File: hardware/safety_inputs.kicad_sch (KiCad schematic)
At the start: 28 parts, among them U11 TLP291-4, U8 TLP291-4, U9 TLP291-4

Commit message: Add the Cube project
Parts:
- added R?: 0R, Resistor_SMD:R_0402_1005Metric, symbol Device:R_Small
- added U10: TCA6416ARTWR, QFN50P400X400X80-25N, symbol TCA6416ARTWR:TCA6416ARTWR
- R? (x12): value 100R -> 2k
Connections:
- net +3.3V: now also U10.21 (VCCP), U10.23 (VCCI)
- net GND: now also R?.1, U10.25 (EP), U10.9 (GND)
- net OUT_ASMS: now also U10.15 (P15)
- net OUT_FW: now also U10.14 (P14)
- net OUT_HV: now also U10.13 (P13)
- net OUT_HVD: now also U10.11 (P11)
- net OUT_INV: now also U10.10 (P10)
- net OUT_RES: now also U10.12 (P12)
- net OUT_RFU1: now also U10.16 (P16)
- net OUT_RFU2: now also U10.17 (P17)
- net OUT_W_FL: now also U10.1 (P00)
- net OUT_W_FR: now also U10.2 (P01)
- net OUT_W_RL: now also U10.3 (P02)
- net OUT_W_RR: now also U10.4 (P03)
- net IN_W_FL renamed IN_WHEEL_FL
- net IN_W_FR renamed IN_WHEEL_FR
- net IN_W_RL renamed IN_WHEEL_RL
- net IN_W_RR renamed IN_WHEEL_RR
- new net: R?.2, U10.18 (ADDR)
- new net LED_CAN: U10.5 (P04)
- new net LED_ERROR: U10.6 (P05)
- new net LED_FUSE: U10.8 (P07)
- new net LED_SAFETY: U10.7 (P06)
- new net SCL: U10.19 (SCL)
- new net SDA: U10.20 (SDA)
- new net ~{INT}: U10.22 (~{INT})
- new net ~{RESET}: U10.24 (~{RESET})
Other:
- note added: "Status LEDs"
- note removed: "ASMS"
- note removed: "FW"
- note removed: "HV"
- note removed: "HVD"
- note removed: "INV"
- note removed: "Larger diode resistor?"
- note removed: "RES"
- note removed: "WHEEL FL"
- note removed: "WHEEL FR"
- note removed: "WHEEL RL"
- note removed: "WHEEL RR"
- title: (none) -> Safety Inputs
- moved on the sheet: R?, U11A, U11B, U11C, U11D, U8A, U8B, U8D, U9A, U9B, U9C, U9D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

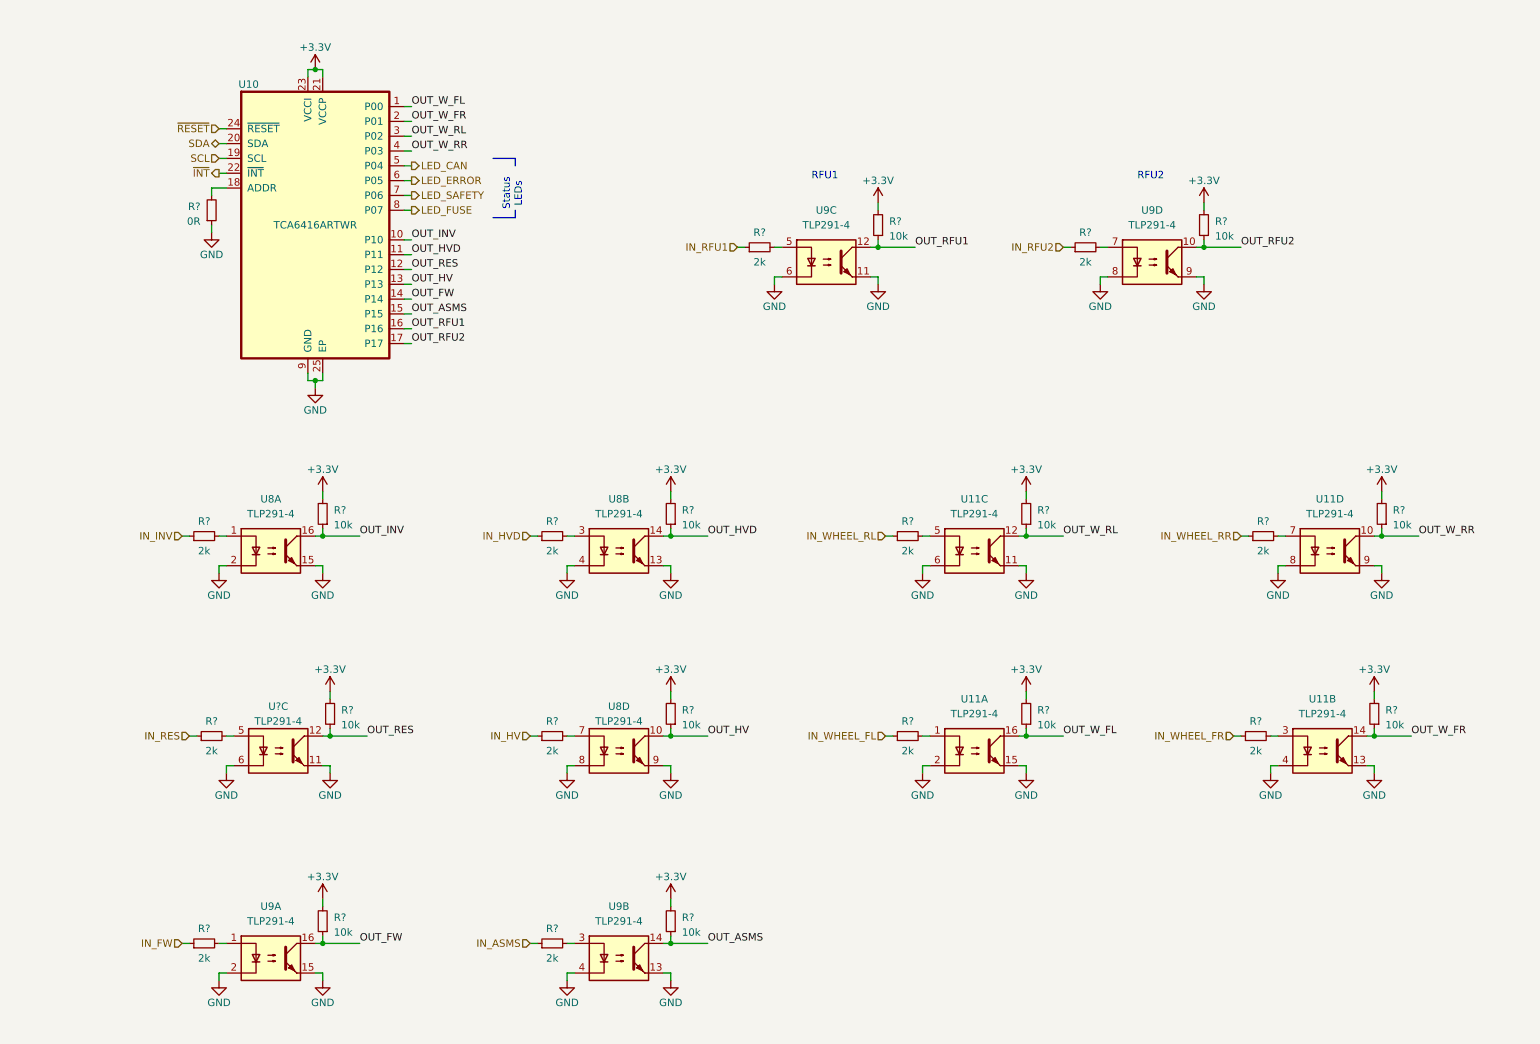
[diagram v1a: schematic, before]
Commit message: Improve the schematic
- add anti-aliasing filters
- rearrange the main connector signals
- improve the power filtering
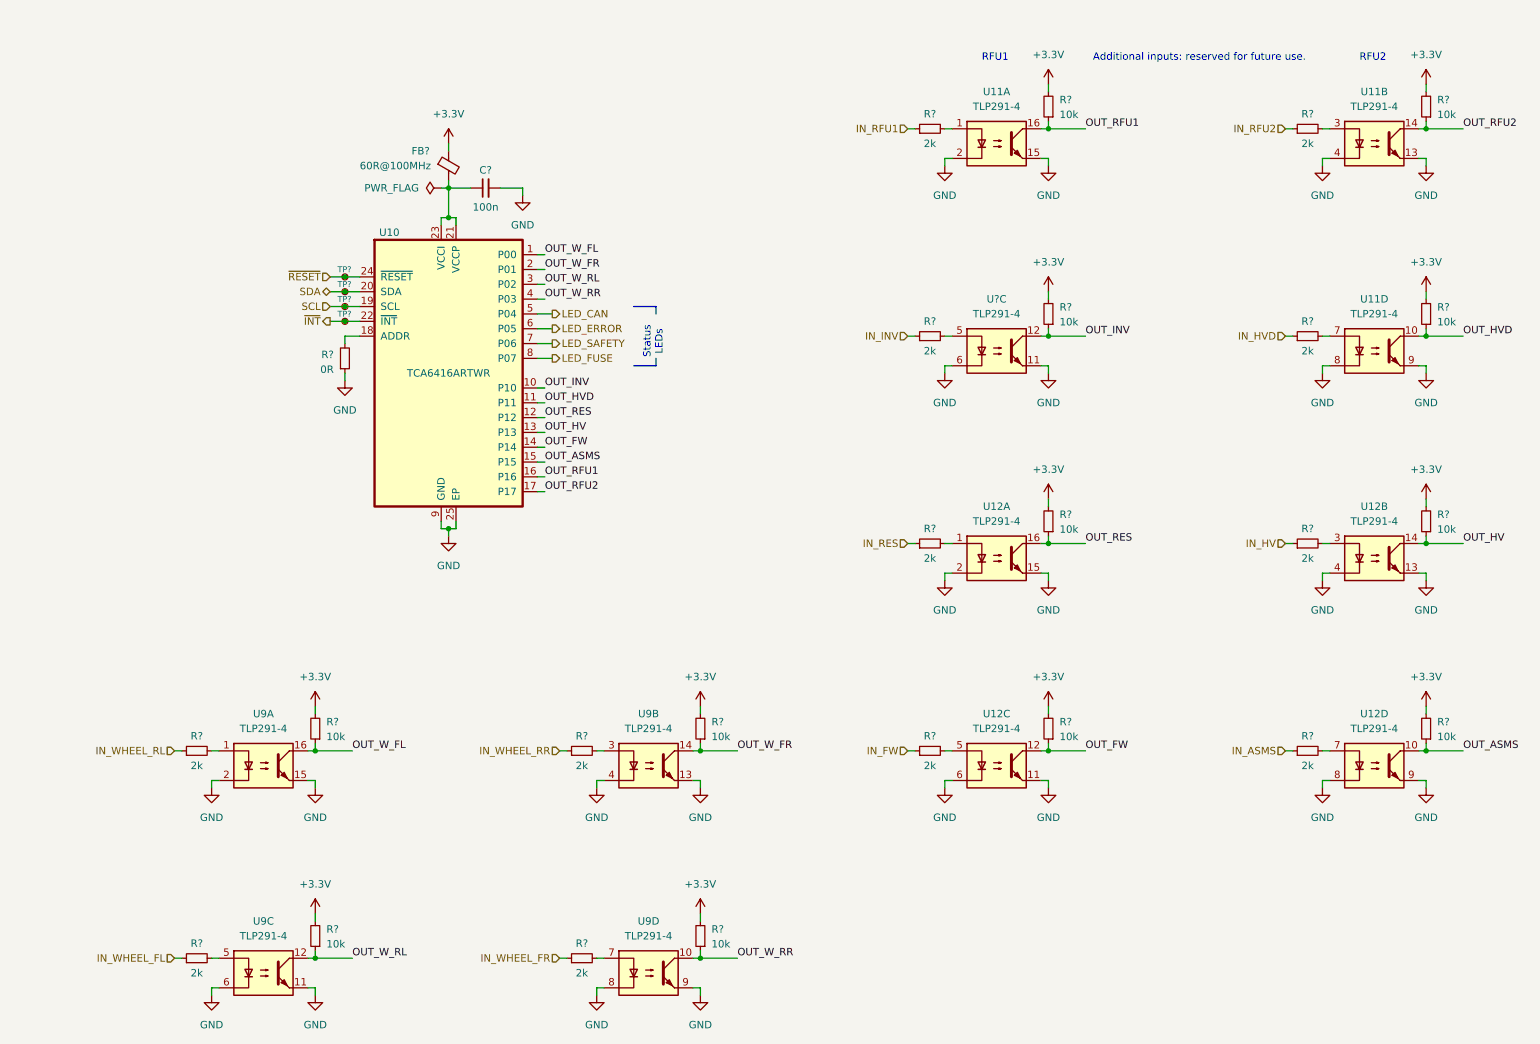
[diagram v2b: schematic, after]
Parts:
- added C?: 100n, Capacitor_SMD:C_0603_1608Metric, symbol Device:C_Small
- added FB?: 60R@100MHz, Inductor_SMD:L_0603_1608Metric, symbol Device:FerriteBead_Small
- added TP? (x4): TestPoint_Small, TestPoint:TestPoint_Pad_D1.0mm, symbol Connector:TestPoint_Small
- R? (x25): footprint Resistor_SMD:R_0402_1005Metric -> Resistor_SMD:R_0603_1608Metric
- renumbered U8 to U11, U9 to U12, U11 to U9
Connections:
- net +3.3V: now also FB?.1; no longer U10.21 (VCCP), U10.23 (VCCI)
- net GND: now also C?.2
- net OUT_ASMS: now also U12.10; no longer U12.14
- net OUT_FW: now also U12.12; no longer U12.16
- net OUT_HV: now also U12.14; no longer U11.10
- net OUT_HVD: now also U11.10; no longer U11.14
- net OUT_INV: now also U?.12; no longer U11.16
- net OUT_RES: now also U12.16; no longer U?.12
- net OUT_RFU1: now also U11.16; no longer U12.12
- net OUT_RFU2: now also U11.14; no longer U12.10
- net OUT_W_FL: now also R?.1; no longer R?.1
- net OUT_W_FR: now also R?.1; no longer R?.1
- net OUT_W_RL: now also R?.1; no longer R?.1
- net OUT_W_RR: now also R?.1; no longer R?.1
- net SCL: now also TP?.1
- net SDA: now also TP?.1
- net ~{INT}: now also TP?.1
- net ~{RESET}: now also TP?.1
- net at R?.2: now also U9.3; no longer U9.7
- net at U12.7: now also R?.2; no longer R?.2
- net at R?.2: now also U12.3; no longer U11.7
- net at U12.1: now also R?.2; no longer R?.2
- net at R?.2: now also U9.5; no longer U9.1
- net at U?.5: now also R?.2; no longer R?.2
- net at R?.2: now also U9.7; no longer U9.3
- net at U11.1: now also R?.2; no longer R?.2
- net at R?.2: now also U9.1; no longer U9.5
- net at R?.2: now also U11.7; no longer U11.3
- net at U12.5: now also R?.2; no longer R?.2
- new net: C?.1, FB?.2, U10.21 (VCCP), U10.23 (VCCI)
- new net: R?.2, U11.3
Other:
- note added: "Additional inputs: reserved for future use."
- moved on the sheet: R?, U10, U11A, U11B, U11D, U12A, U12B, U12C, U12D, U9A, U9B, U9C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

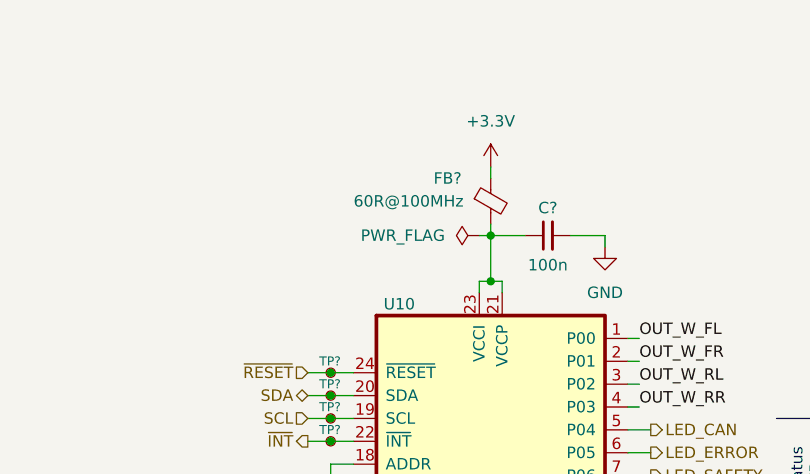
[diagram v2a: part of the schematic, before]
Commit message: Set component values
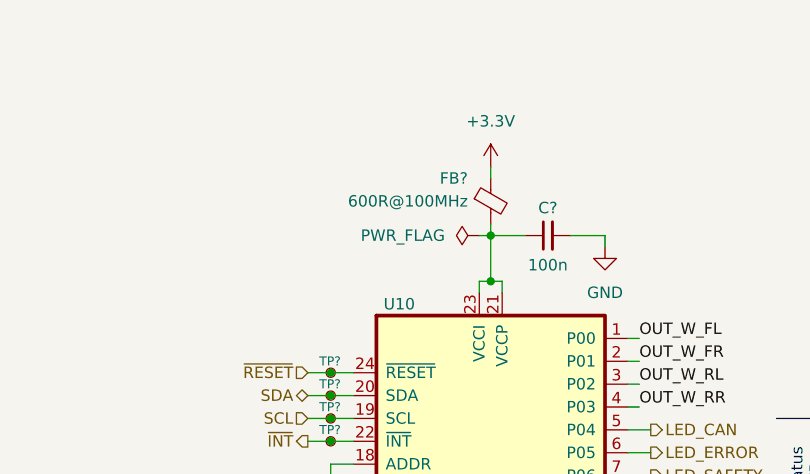
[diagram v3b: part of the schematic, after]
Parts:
- FB?: value 60R@100MHz -> 600R@100MHz
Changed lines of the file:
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@@
         )
         (path "/b652b05a-4e3d-4ad1-b032-18886abe7d45/5d9671f9-6e77-4376-b4d6-afe9f66a07c2"
-          (reference "R59") (unit 1)
+          (reference "R61") (unit 1)
         )
       )
@@
         )
         (path "/b652b05a-4e3d-4ad1-b032-18886abe7d45/5d9671f9-6e77-4376-b4d6-afe9f66a07c2"
-          (reference "R73") (unit 1)
+          (reference "R75") (unit 1)
         )
       )
@@
   (symbol (lib_id "Device:FerriteBead_Small") (at 91.44 43.18 0) (unit 1)
     (in_bom yes) (on_board yes) (dnp no)
-    (property "Reference" "FB?" (at 85.09 40.64 0)
-      (effects (font (size 1.27 1.27)) (justify left))
-    )
-    (property "Value" "60R@100MHz" (at 76.2 43.18 0)
-      (effects (font (size 1.27 1.27)) (justify left))
+    (property "Reference" "FB?" (at 88.9 40.64 0)
+      (effects (font (size 1.27 1.27)) (justify right))
+    )
+    (property "Value" "600R@100MHz" (at 88.9 43.18 0)
+      (effects (font (size 1.27 1.27)) (justify right))
     )
     (property "Footprint" "Inductor_SMD:L_0603_1608Metric" (at 89.662 43.18 90)
@@
         )
         (path "/b652b05a-4e3d-4ad1-b032-18886abe7d45/5d9671f9-6e77-4376-b4d6-afe9f66a07c2"
-          (reference "R55") (unit 1)
+          (reference "R57") (unit 1)
         )
       )
@@
         )
         (path "/b652b05a-4e3d-4ad1-b032-18886abe7d45/5d9671f9-6e77-4376-b4d6-afe9f66a07c2"
-          (reference "R78") (unit 1)
+          (reference "R80") (unit 1)
         )
       )
@@
         )
         (path "/b652b05a-4e3d-4ad1-b032-18886abe7d45/5d9671f9-6e77-4376-b4d6-afe9f66a07c2"
-          (reference "R65") (unit 1)
+          (reference "R67") (unit 1)
         )
       )
@@
         )
         (path "/b652b05a-4e3d-4ad1-b032-18886abe7d45/5d9671f9-6e77-4376-b4d6-afe9f66a07c2"
-          (reference "R68") (unit 1)
+          (reference "R70") (unit 1)
         )
       )
@@
         )
         (path "/b652b05a-4e3d-4ad1-b032-18886abe7d45/5d9671f9-6e77-4376-b4d6-afe9f66a07c2"
-          (reference "R76") (unit 1)
+          (reference "R78") (unit 1)
         )
       )
@@
         )
         (path "/b652b05a-4e3d-4ad1-b032-18886abe7d45/5d9671f9-6e77-4376-b4d6-afe9f66a07c2"
-          (reference "C34") (unit 1)
+          (reference "C35") (unit 1)
         )
       )
@@
         )
         (path "/b652b05a-4e3d-4ad1-b032-18886abe7d45/5d9671f9-6e77-4376-b4d6-afe9f66a07c2"
-          (reference "R60") (unit 1)
+          (reference "R62") (unit 1)
         )
       )
@@
         )
         (path "/b652b05a-4e3d-4ad1-b032-18886abe7d45/5d9671f9-6e77-4376-b4d6-afe9f66a07c2"
-          (reference "R64") (unit 1)
+          (reference "R66") (unit 1)
         )
       )
@@
         )
         (path "/b652b05a-4e3d-4ad1-b032-18886abe7d45/5d9671f9-6e77-4376-b4d6-afe9f66a07c2"
-          (reference "R61") (unit 1)
+          (reference "R63") (unit 1)
         )
       )
@@
         )
         (path "/b652b05a-4e3d-4ad1-b032-18886abe7d45/5d9671f9-6e77-4376-b4d6-afe9f66a07c2"
-          (reference "R54") (unit 1)
+          (reference "R56") (unit 1)
         )
       )
@@
         )
         (path "/b652b05a-4e3d-4ad1-b032-18886abe7d45/5d9671f9-6e77-4376-b4d6-afe9f66a07c2"
-          (reference "R57") (unit 1)
+          (reference "R59") (unit 1)
         )
       )
@@
         )
         (path "/b652b05a-4e3d-4ad1-b032-18886abe7d45/5d9671f9-6e77-4376-b4d6-afe9f66a07c2"
-          (reference "R70") (unit 1)
+          (reference "R72") (unit 1)
         )
       )
@@
         )
         (path "/b652b05a-4e3d-4ad1-b032-18886abe7d45/5d9671f9-6e77-4376-b4d6-afe9f66a07c2"
-          (reference "R72") (unit 1)
+          (reference "R74") (unit 1)
         )
       )
@@
         )
         (path "/b652b05a-4e3d-4ad1-b032-18886abe7d45/5d9671f9-6e77-4376-b4d6-afe9f66a07c2"
-          (reference "R63") (unit 1)
+          (reference "R65") (unit 1)
         )
       )
@@
         )
         (path "/b652b05a-4e3d-4ad1-b032-18886abe7d45/5d9671f9-6e77-4376-b4d6-afe9f66a07c2"
-          (reference "R58") (unit 1)
+          (reference "R60") (unit 1)
         )
       )
@@
         )
         (path "/b652b05a-4e3d-4ad1-b032-18886abe7d45/5d9671f9-6e77-4376-b4d6-afe9f66a07c2"
-          (reference "R71") (unit 1)
+          (reference "R73") (unit 1)
         )
       )
@@
         )
         (path "/b652b05a-4e3d-4ad1-b032-18886abe7d45/5d9671f9-6e77-4376-b4d6-afe9f66a07c2"
-          (reference "R67") (unit 1)
+          (reference "R69") (unit 1)
         )
       )
@@
         )
         (path "/b652b05a-4e3d-4ad1-b032-18886abe7d45/5d9671f9-6e77-4376-b4d6-afe9f66a07c2"
-          (reference "R75") (unit 1)
+          (reference "R77") (unit 1)
         )
       )
@@
         )
         (path "/b652b05a-4e3d-4ad1-b032-18886abe7d45/5d9671f9-6e77-4376-b4d6-afe9f66a07c2"
-          (reference "R69") (unit 1)
+          (reference "R71") (unit 1)
         )
       )
@@
         )
         (path "/b652b05a-4e3d-4ad1-b032-18886abe7d45/5d9671f9-6e77-4376-b4d6-afe9f66a07c2"
-          (reference "R74") (unit 1)
+          (reference "R76") (unit 1)
         )
       )
@@
         )
         (path "/b652b05a-4e3d-4ad1-b032-18886abe7d45/5d9671f9-6e77-4376-b4d6-afe9f66a07c2"
-          (reference "R56") (unit 1)
+          (reference "R58") (unit 1)
         )
       )
@@
         )
         (path "/b652b05a-4e3d-4ad1-b032-18886abe7d45/5d9671f9-6e77-4376-b4d6-afe9f66a07c2"
-          (reference "R77") (unit 1)
+          (reference "R79") (unit 1)
         )
       )
@@
         )
         (path "/b652b05a-4e3d-4ad1-b032-18886abe7d45/5d9671f9-6e77-4376-b4d6-afe9f66a07c2"
-          (reference "R62") (unit 1)
+          (reference "R64") (unit 1)
         )
       )
@@
         )
         (path "/b652b05a-4e3d-4ad1-b032-18886abe7d45/5d9671f9-6e77-4376-b4d6-afe9f66a07c2"
-          (reference "R66") (unit 1)
-        )
-      )
+          (reference "R68") (unit 1)
+        )
+      )
